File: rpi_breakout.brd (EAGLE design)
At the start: 34.4 x 38.4 mm, 21 parts

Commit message: Beefed up everything, made board partial CC size
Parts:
- moved JP8 15.1 mm to (21.9, 25.7)
- moved LED3 15.1 mm to (25.7, 23.2)
- moved LED4 15.1 mm to (25.6, 25.7)
- moved JP7 15.1 mm to (21.9, 23.3)
- moved R4 15.1 mm to (23.4, 27.6)
- moved C1 15.1 mm to (6.96, 21.3)
- moved JP5 15.1 mm to (2.34, 40.4)
- moved JP6 15.1 mm to (2.48, 20.5)
- moved LED1 15.1 mm to (4.56, 33.9)
- moved LED2 15.1 mm to (4.54, 31.7)
- moved R2 15.1 mm to (8.16, 31.7)
- moved U2 15.1 mm to (16.9, 32.0)
- moved VREG1 15.1 mm to (7.47, 23.7)
- moved C2 15.1 mm to (7.03, 27.4)
- moved JP1 15.1 mm to (16.5, 50.8)
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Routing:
- net VCC: track 81.6 -> 101.2 mm
- net GPIO_7: track 28.8 -> 21.3 mm, vias 0 -> 1
- net GPIO_6: track 25.6 -> 32.5 mm, vias 1 -> 0
- net SPI_SCLK: track 16.2 -> 12.8 mm, vias 0 -> 1
- net /SPI_CE1: track 28.8 -> 25.5 mm
- net TXDV: track 9.87 -> 6.66 mm
- net GPIO_0: track 14.8 -> 12.5 mm
- net 3V3_RPI: track 62.1 -> 59.9 mm
- net GPIOV_4: track 13.1 -> 15.1 mm
- net GPIOV_5: track 13.3 -> 15.2 mm
- net GPIOV_6: track 13.9 -> 15.8 mm
- net GPIOV_7: track 14.0 -> 15.9 mm
- net GPIOV_3: track 12.8 -> 14.6 mm
- net SPI_SCLKV: track 8.69 -> 6.95 mm
- net GND: track 97.0 -> 95.3 mm, vias 0 -> 1
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- removed copper zone on layer 1, net GND
- removed copper zone on layer 16, net VCC
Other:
- board size 34.4 x 38.4 mm -> 33 x 54 mm

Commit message: Fatter still, handrouted, with funky Vcc polygons.  Probably won't want to use this one.
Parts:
- moved JP3 28.9 mm to (2.57, 13.0), turned to 0 degrees
- moved JP2 25.9 mm to (31.5, 41.7), turned to 270 degrees
- moved JP4 22.3 mm to (18.0, 13.0), turned to 0 degrees
- moved U3 12.8 mm to (15.7, 29.0), turned to 180 degrees
- moved U2 9.16 mm to (21.9, 39.6)
- moved JP5 2.16 mm to (2.42, 42.5)
- moved R3 0.13 mm to (23.8, 21.0)
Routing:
- net GND: track 95.3 -> 127.2 mm, vias 1 -> 0
- net 3.3V: track 35.3 -> 11.9 mm
- net /SPI_CE1: track 25.5 -> 46.6 mm
- net SPI_MOSI: track 9.95 -> 27.9 mm
- net GPIO_6: track 32.5 -> 16.8 mm, vias 0 -> 1
- net /SPI_CE0: track 17.0 -> 30.9 mm
- net VCC: track 101.2 -> 87.7 mm
- net RXDV: track 7.10 -> 19.0 mm
- net GPIOV_0: track 18.3 -> 6.84 mm
- net TXDV: track 6.66 -> 17.3 mm
- net SPI_MISO: track 12.1 -> 22.3 mm
- net SPI_SCLKV: track 6.95 -> 17.1 mm
- net SPI_SCLK: track 12.8 -> 22.8 mm, vias 1 -> 0
- net GPIO_3: track 18.1 -> 8.14 mm, vias 1 -> 0
- net GPIOV_1: track 16.6 -> 6.83 mm
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- added copper zone on layer 1, net GND
- added copper zone on layer 16, net N$3
- added copper zone on layer 1, net VCC

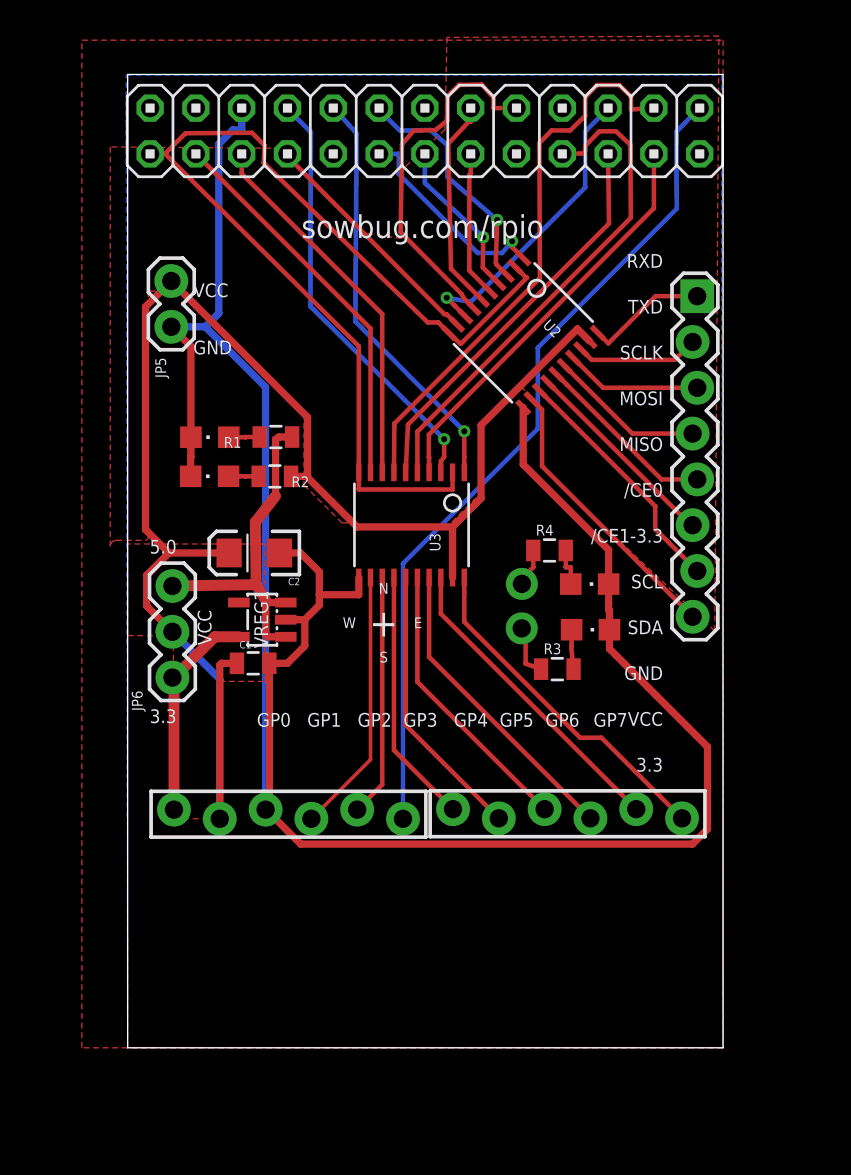
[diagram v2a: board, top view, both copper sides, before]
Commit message: Smaller board footprint again; Merged from canton7's nice layout
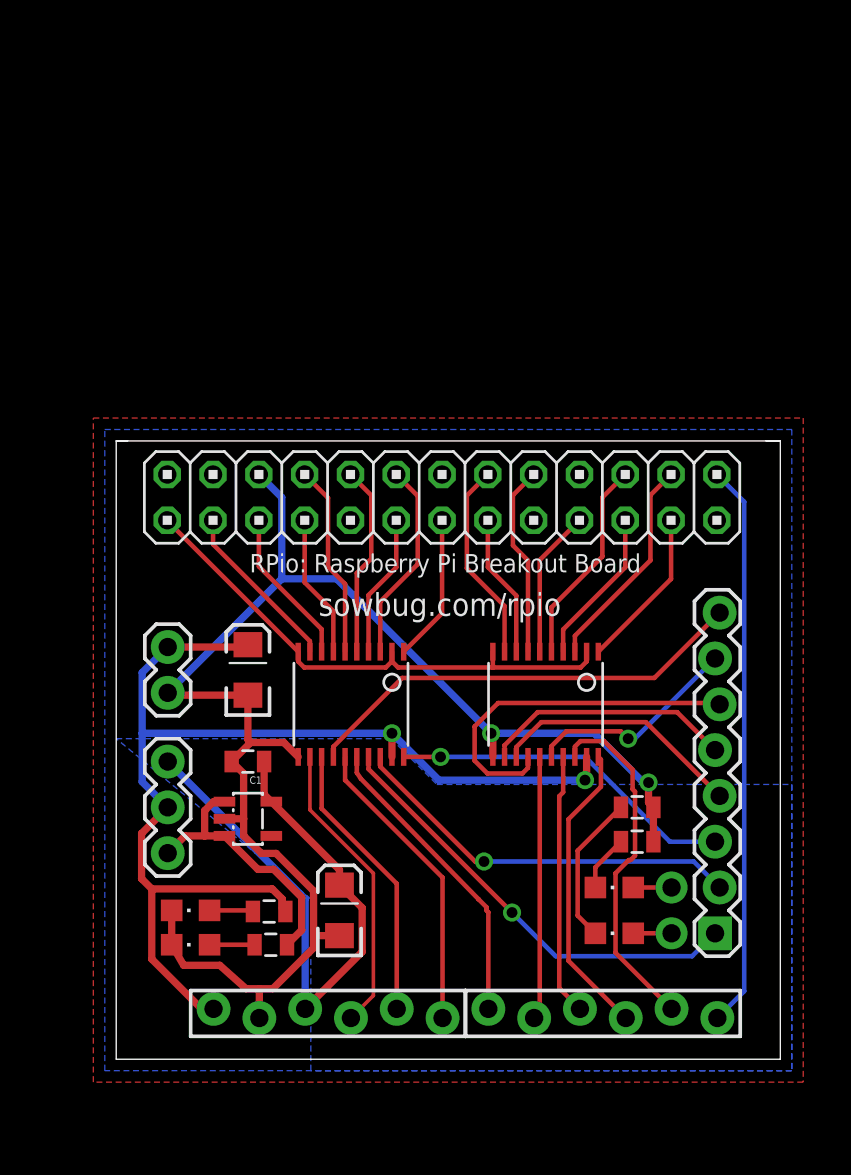
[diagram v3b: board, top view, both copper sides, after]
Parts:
- added C3: 10uF, SparkFun:EIA3216
- JP2: device SparkFun:1X08_LOCK -> rpi_breakout:1X08_LOCK
- U2, U3: device adafruit:TSSOP20 -> rpi_breakout:TSSOP20
- moved JP2 35.4 mm to (32.7, 6.35), turned to 90 degrees
- moved LED1 28.2 mm to (3.49, 5.71)
- moved R1 28.2 mm to (7.94, 5.71)
- moved R2 24.1 mm to (7.85, 7.56)
- moved LED2 24.1 mm to (3.49, 7.62)
- moved JP8 21.1 mm to (30.2, 6.35)
- moved U2 20.6 mm to (23.2, 19.1), turned to 180 degrees
- moved C2 20.4 mm to (11.7, 7.62), turned to 90 degrees
- moved JP1 20.3 mm to (17.4, 30.5)
- moved JP5 20.3 mm to (2.22, 22.2)
- moved LED4 19.4 mm to (27.0, 6.35), turned to 90 degrees
- moved JP7 16.6 mm to (30.2, 8.89)
- moved R4 15.1 mm to (28.3, 13.3)
- moved LED3 14.4 mm to (27.0, 8.89), turned to 90 degrees
- moved JP3 11.3 mm to (4.76, 1.91)
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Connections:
- removed net LED3_A: LED3.A, R3.2
- removed net LED4_A: LED4.A, R4.2
- new net N$3: LED3.C, R3.1
- new net N$4: LED4.C, R4.1
- net /SPI_CE0: now also U2.3; no longer U3.7
- net /SPI_CE1: now also JP4.6; no longer JP3.6
- net /SPI_CEV0: now also JP4.5, U2.18; no longer JP4.1, U3.14
- net 3.3V: now also C1.1, C2.A, JP3.3; no longer JP3.1
- net GND: now also C3.C, JP3.2, R3.2, R4.2; no longer JP3.3, LED3.C, LED4.C
- net GPIOV_0: now also U3.17; no longer U2.20
- net GPIOV_1: now also U3.18; no longer U2.18
- net GPIOV_2: now also U3.20; no longer U2.17
- net GPIOV_3: now also U2.13; no longer U2.16
- net GPIOV_4: now also U2.12; no longer U2.15
- net GPIOV_6: now also U2.16; no longer U2.13
- net GPIOV_7: now also U3.14; no longer U2.12
- net GPIO_0: now also U3.4; no longer U2.1
- net GPIO_1: now also U3.3; no longer U2.3
- net GPIO_2: now also U3.1; no longer U2.4
- net GPIO_3: now also U2.8; no longer U2.5
- net GPIO_4: now also U2.9; no longer U2.6
- net GPIO_6: now also U2.5; no longer U2.8
- net GPIO_7: now also U3.7; no longer U2.9
- net LED3_JP: now also LED3.A; no longer R3.1
- net LED4_JP: now also LED4.A; no longer R4.1
- net RXD: now also U3.5; no longer U3.1
- net RXDV: now also JP4.1, U3.16; no longer JP4.6, U3.20
- net SPI_MISO: now also U2.4; no longer U3.6
- net SPI_MISOV: now also JP4.3, U2.17; no longer JP4.2, U3.15
- net SPI_MOSI: now also U2.6; no longer U3.5
- net SPI_MOSIV: now also JP4.2, U2.15; no longer JP4.3, U3.16
- net SPI_SCLK: now also U2.1; no longer U3.4
- net SPI_SCLKV: now also U2.20; no longer U3.17
- net TXD: now also U3.6; no longer U3.3
- net TXDV: now also JP3.6, U3.15; no longer JP4.5, U3.18
- net VCC: now also C3.A, JP3.1; no longer C1.1, C2.A, JP3.2
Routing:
- net GND: track 127.2 -> 85.3 mm, vias 0 -> 2
- net 3V3_RPI: track 58.6 -> 29.3 mm
- net VCC: track 87.7 -> 64.9 mm, vias 0 -> 2
- net 3.3V: track 11.9 -> 34.2 mm
- net SPI_MOSI: track 27.9 -> 8.20 mm
- net /SPI_CE0: track 30.9 -> 12.0 mm
- net GPIOV_0: track 6.84 -> 24.7 mm, vias 0 -> 1
- net GPIOV_1: track 6.83 -> 22.1 mm, vias 0 -> 1
- net /SPI_CE1: track 46.6 -> 31.4 mm
- net SPI_SCLK: track 22.8 -> 8.96 mm
- net SPI_MISO: track 22.3 -> 8.71 mm
- net TXD: track 23.9 -> 10.8 mm, vias 1 -> 0
- net RXD: track 23.5 -> 10.6 mm, vias 1 -> 0
- net SCL0: track 20.9 -> 8.73 mm
- net SDA0: track 21.7 -> 9.51 mm
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- added copper zone on layer 16, net GND
- added copper zone on layer 16, net VCC
- removed copper zone on layer 16, net N$3
- removed copper zone on layer 1, net VCC
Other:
- board size 33 x 54 mm -> 36.8 x 34.3 mm
- board text removed: "+"
- board text removed: "/CE0"
- board text removed: "/CE1-3.3"
- board text removed: "3.3"
- board text removed: "5.0"
- board text removed: "DANGER: CE1 is always 3.3V!"
- board text removed: "E"
- board text removed: "GND"
- board text removed: "GP0"
- board text removed: "GP1"
- board text removed: "GP2"
- board text removed: "GP3"
- board text removed: "GP4"
- board text removed: "GP5"
- board text removed: "GP6"
- board text removed: "GP7"
- board text removed: "MISO"
- board text removed: "MOSI"
- board text removed: "N"
- board text removed: "RXD"
- board text removed: "S"
- board text removed: "SCL"
- board text removed: "SCLK"
- board text removed: "SDA"
- board text removed: "TXD"
- board text removed: "VCC"
- board text removed: "W"
- board text removed: "sowbug.com"
- board text removed: "v0.0.2"
